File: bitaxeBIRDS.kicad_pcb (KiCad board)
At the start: 6 copper layers, 65 x 112 mm, 194 parts, among them J1 XT30, J2 USB_C_Receptacle_USB2.0, J3 Conn_01x04, J4 Conn_01x04, SW1 SWITCH-SPST, SW2 SWITCH-SPST, U1 TPSM861253RDXR, U12 TLV75512PDQNR, U13 EMC2103-2, U14 TLV75512PDQNR, U15 TLV75512PDQNR, U2 TPS546D24ARVFR, U3 TLV75512PDQNR, U4 W25Q16JVUXIQ TR, U5 TPS22919DCKR, U6 RP2040, U7 SK6812, U8 SN74AVC4T774, Y1 12MHz, Y2 50MHz

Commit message: more routing
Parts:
- moved C59 39.6 mm to (127.5, 105.2)
- moved C57 38.4 mm to (125.2, 106.8), turned to -90 degrees
- moved R19 36.2 mm to (103.7, 72.7)
- moved R6 35.1 mm to (130.4, 78.0), turned to 180 degrees
- moved R26 34.7 mm to (127.2, 101.6), turned to 90 degrees
- moved U8 31.9 mm to (124.7, 103.6), turned to 0 degrees
- moved TP14 31.2 mm to (137.0, 108.9), turned to 0 degrees
- moved TP11 30.7 mm to (137.0, 99.8), turned to 0 degrees
- moved C17 30.4 mm to (134.0, 78.0), turned to 180 degrees
- moved TP13 29.8 mm to (137.0, 105.9), turned to 0 degrees
- moved TP12 29.7 mm to (137.0, 102.8), turned to 0 degrees
- moved R45 19.2 mm to (152.5, 128.3), turned to -90 degrees
- moved R46 19.0 mm to (151.9, 129.8), turned to 180 degrees
- moved C27 19.0 mm to (152.6, 103.3)
- moved C28 19.0 mm to (150.7, 104.9)
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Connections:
- net Net-(R18-Pad2) renamed /Data/MCU_BOOT
- net Net-(U6-RUN) renamed /Data/MCU_RESET
- U6 pad 2: /Data/PWR_EN -> /Power/PWR_EN
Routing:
- net /5V_SWITCH: track 0.01 -> 150.4 mm, vias 0 -> 7
- net /3V3: track 104.3 -> 28.6 mm, vias 36 -> 31
- net /ASIC/TRIP_3V3: track 0.00 -> 61.9 mm, vias 0 -> 2
- net /Data/SCL: track 116.3 -> 175.9 mm, vias 3 -> 4
- net /5V: track 74.0 -> 14.9 mm
- net /Data/SDA: track 118.6 -> 174.1 mm, vias 3 -> 4
- net /ASIC/RX_3V3: track 6.42 -> 60.9 mm
- net /ASIC/RST_3V3: track 4.01 -> 58.3 mm
- net /ASIC/TX_3V3: track 8.36 -> 61.3 mm
- net /Power/PGOOD: track 13.3 -> 58.8 mm, vias 0 -> 2
- net /Power/SMB_ALRT: track 13.0 -> 57.0 mm, vias 0 -> 2
- net /ASIC/1V2-2: track 0.00 -> 23.7 mm, vias 0 -> 4
- net /ASIC/shifter1-2/TRIP_OUT: track 0.00 -> 21.0 mm, vias 0 -> 1
- net /ASIC/shifter1-2/TX_OUT: track 0.00 -> 19.8 mm, vias 0 -> 1
- net /ASIC/shifter1-2/RESET_IN: track 0.00 -> 18.6 mm, vias 0 -> 1
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- added copper zone on B.Cu, net /12V
- added copper zone on F.Cu, net /ASIC/GND4

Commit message: more routing
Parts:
- moved TP8 25.0 mm to (127.7, 64.7)
- moved TP9 24.0 mm to (125.3, 64.7)
- moved TP1 6.39 mm to (126.6, 55.2)
- moved TP4 4.83 mm to (153.3, 107.0)
- moved C10 1.30 mm to (143.3, 68.9), turned to 90 degrees
- moved C76 1.29 mm to (123.0, 144.4)
- moved C11 0.38 mm to (141.7, 69.0)
- moved C17 0.09 mm to (134.0, 77.9)
- moved R5 0.07 mm to (140.1, 68.3), turned to -90 degrees
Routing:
- net /3V3: track 28.6 -> 206.2 mm, vias 31 -> 33
- net /5V: track 14.9 -> 140.1 mm
- net /Data/MCU_BOOT: track 0.00 -> 55.1 mm, vias 1 -> 3
- net /ASIC/REFCLKOUT2: track 0.00 -> 43.1 mm, vias 0 -> 1
- net /ASIC/GND2: track 17.4 -> 56.2 mm, vias 18 -> 21
- net /fan/FAN_PWM: track 1.49 -> 29.7 mm, vias 0 -> 1
- net /5V_SWITCH: track 150.4 -> 177.9 mm
- net /Power/PWR_EN: track 1.40 -> 28.8 mm, vias 1 -> 3
- net /ASIC/GND3: track 10.8 -> 37.2 mm, vias 6 -> 9
- net /fan/FAN_TACH: track 1.99 -> 26.7 mm, vias 0 -> 1
- net /ASIC/1V2-1: track 15.8 -> 40.1 mm, vias 5 -> 7
- net /ASIC/1V2-3: track 6.28 -> 28.3 mm
- net /ASIC/GND4: track 3.66 -> 25.6 mm, vias 4 -> 5
- net /Data/MCU_RESET: track 1.48 -> 22.7 mm
- net /ASIC/1V2-4: track 3.79 -> 13.2 mm
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
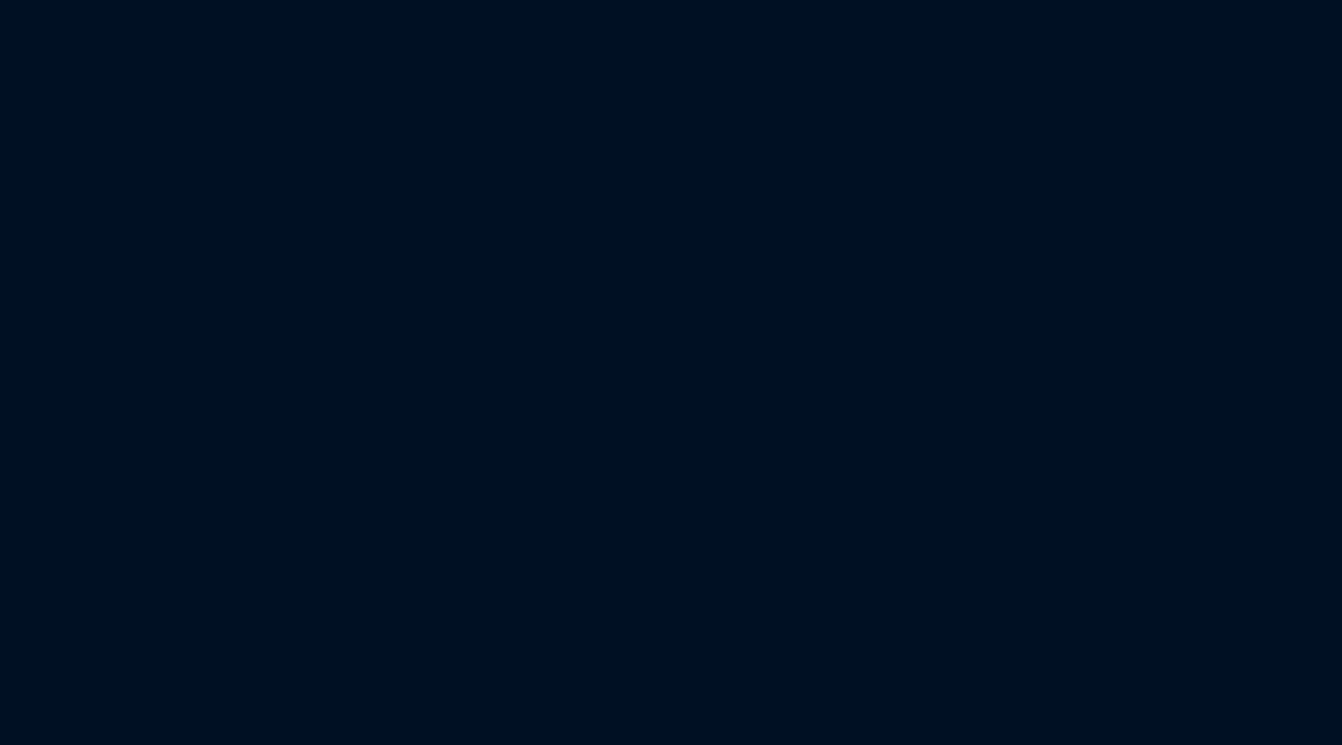
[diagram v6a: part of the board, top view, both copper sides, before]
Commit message: Added RP Pico W2 to schematic. Fixed Domain 1-2 level shifter pins. Added test points
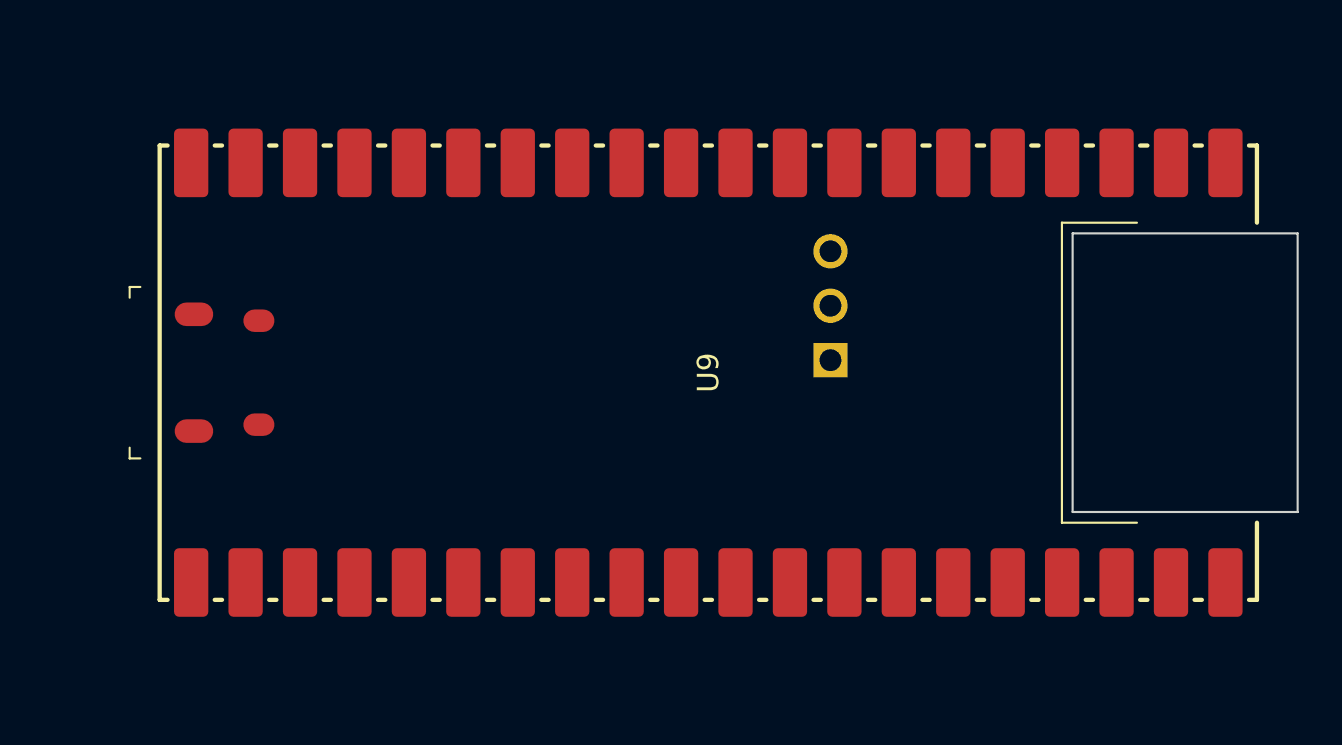
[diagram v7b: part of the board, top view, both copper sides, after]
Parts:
- added U9: Raspberry Pi Pico, bitaxe:RasPi_Pico_W_SMD, F.Cu at (198.3, 71.7)
